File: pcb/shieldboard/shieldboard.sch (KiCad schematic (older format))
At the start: 48 parts

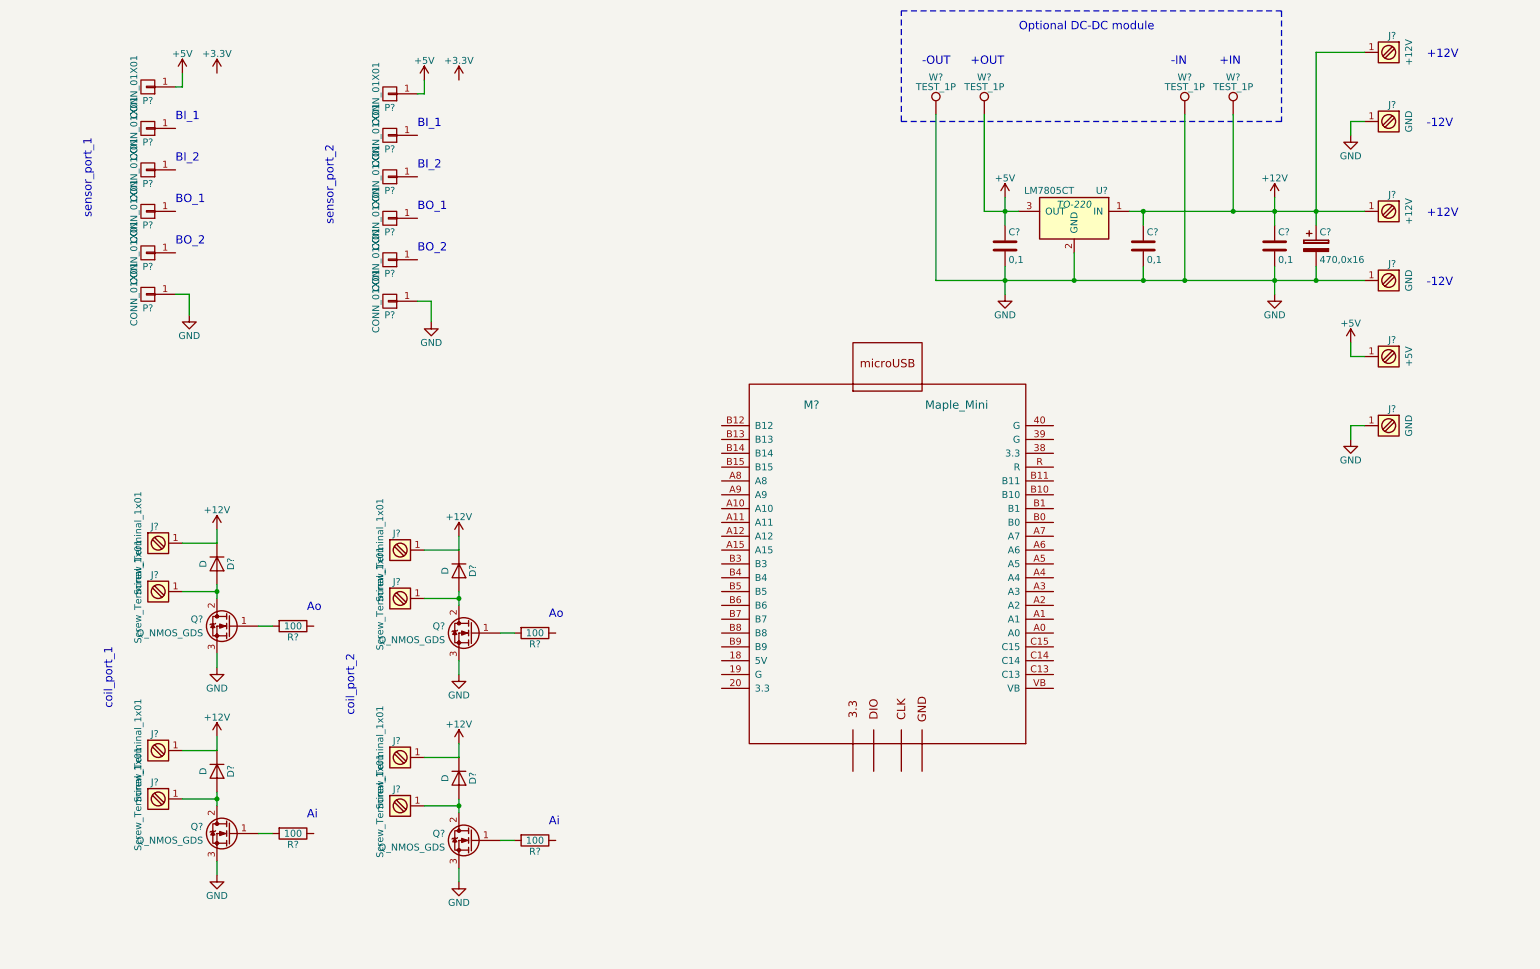
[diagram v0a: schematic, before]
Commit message: pcb: connect uC board to the shield
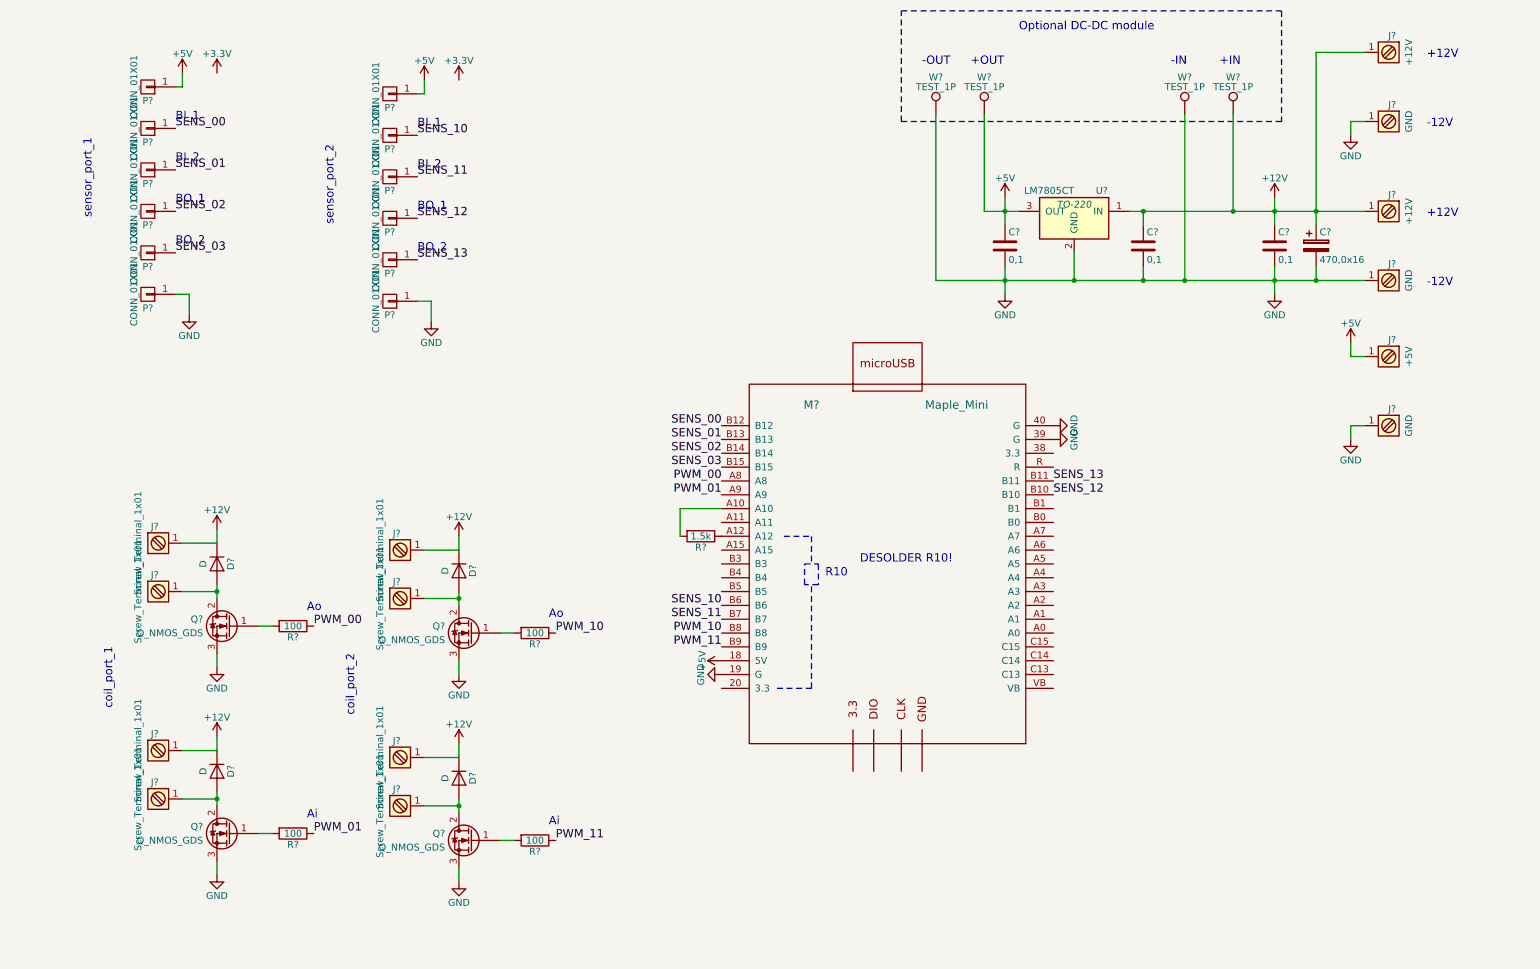
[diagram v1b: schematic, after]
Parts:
- added R?: 1.5k, symbol R
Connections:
- net +5V: now also M?.18 (5V)
- net GND: now also M?.19 (G), M?.39 (G), M?.40 (G)
- net SENS_02: now reaches P?.1 (P1)
- net SENS_02: now also M?.B14
- net SENS_01: now reaches P?.1 (P1)
- net SENS_01: now also M?.B13
- net SENS_00: now reaches P?.1 (P1)
- net SENS_00: now also M?.B12
- net SENS_03: now reaches P?.1 (P1)
- net SENS_03: now also M?.B15
- net PWM_00: now reaches R?.1
- net PWM_00: now also M?.A8
- net PWM_01: now reaches R?.1
- net PWM_01: now also M?.A9
- net at M?.A10: now also R?.2
- net at M?.A12: now also R?.1
- net SENS_12: now reaches M?.B10
- net SENS_12: now also P?.1 (P1)
- net SENS_13: now reaches M?.B11
- net SENS_13: now also P?.1 (P1)
- net SENS_10: now reaches M?.B6
- net SENS_10: now also P?.1 (P1)
- net SENS_11: now reaches M?.B7
- net SENS_11: now also P?.1 (P1)
- net PWM_10: now reaches M?.B8
- net PWM_10: now also R?.1
- net PWM_11: now reaches M?.B9
- net PWM_11: now also R?.1
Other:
- note added: "DESOLDER R10!"
- note added: "R10"
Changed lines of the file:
@@
 LIBS:memory
 LIBS:xilinx
+LIBS:special
 LIBS:microcontrollers
 LIBS:dsp
@@
 Wire Wire Line
 	10200 3350 10200 3250
+Text Label 5650 4250 2    60   ~ 0
+PWM_00
+Text Label 5650 4350 2    60   ~ 0
+PWM_01
+Text Label 5650 5350 2    60   ~ 0
+PWM_10
+Text Label 5650 5450 2    60   ~ 0
+PWM_11
+Text Label 5650 3850 2    60   ~ 0
+SENS_00
+Text Label 5650 3950 2    60   ~ 0
+SENS_01
+Text Label 5650 4050 2    60   ~ 0
+SENS_02
+Text Label 5650 4150 2    60   ~ 0
+SENS_03
+Text Label 5650 5150 2    60   ~ 0
+SENS_10
+Text Label 5650 5250 2    60   ~ 0
+SENS_11
+Text Label 8050 4350 0    60   ~ 0
+SENS_12
+Text Label 8050 4250 0    60   ~ 0
+SENS_13
+Text Label 1700 1700 0    60   ~ 0
+SENS_00
+Text Label 1700 2000 0    60   ~ 0
+SENS_01
+Text Label 1700 2300 0    60   ~ 0
+SENS_02
+Text Label 1700 2600 0    60   ~ 0
+SENS_03
+Text Label 3450 1750 0    60   ~ 0
+SENS_10
+Text Label 3450 2050 0    60   ~ 0
+SENS_11
+Text Label 3450 2350 0    60   ~ 0
+SENS_12
+Text Label 3450 2650 0    60   ~ 0
+SENS_13
+Text Label 2700 5300 0    60   ~ 0
+PWM_00
+Text Label 2700 6800 0    60   ~ 0
+PWM_01
+Text Label 4450 6850 0    60   ~ 0
+PWM_11
+Text Label 4450 5350 0    60   ~ 0
+PWM_10
+$Comp
+L GND #PWR?
+U 1 1 5B209E40
+P 8050 3850
+F 0 "#PWR?" H 8050 3600 50  0001 C CNN
+F 1 "GND" H 8050 3700 50  0000 C CNN
+F 2 "" H 8050 3850 50  0000 C CNN
+F 3 "" H 8050 3850 50  0000 C CNN
+	1    8050 3850
+	0    -1   -1   0
+$EndComp
+$Comp
+L GND #PWR?
+U 1 1 5B209EE2
+P 8050 3950
+F 0 "#PWR?" H 8050 3700 50  0001 C CNN
+F 1 "GND" H 8050 3800 50  0000 C CNN
+F 2 "" H 8050 3950 50  0000 C CNN
+F 3 "" H 8050 3950 50  0000 C CNN
+	1    8050 3950
+	0    -1   -1   0
+$EndComp
+$Comp
+L GND #PWR?
+U 1 1 5B20A0CF
+P 5650 5650
+F 0 "#PWR?" H 5650 5400 50  0001 C CNN
+F 1 "GND" H 5650 5500 50  0000 C CNN
+F 2 "" H 5650 5650 50  0000 C CNN
+F 3 "" H 5650 5650 50  0000 C CNN
+	1    5650 5650
+	0    1    1    0
+$EndComp
+$Comp
+L +5V #PWR?
+U 1 1 5B20D291
+P 5650 5550
+F 0 "#PWR?" H 5650 5400 50  0001 C CNN
+F 1 "+5V" H 5650 5690 50  0000 C CNN
+F 2 "" H 5650 5550 50  0000 C CNN
+F 3 "" H 5650 5550 50  0000 C CNN
+	1    5650 5550
+	0    -1   -1   0
+$EndComp
+$Comp
+L R R?
+U 1 1 5B20E5A1
+P 5500 4650
+F 0 "R?" V 5580 4650 50  0000 C CNN
+F 1 "1.5k" V 5500 4650 50  0000 C CNN
+F 2 "" V 5430 4650 50  0000 C CNN
+F 3 "" H 5500 4650 50  0000 C CNN
+	1    5500 4650
+	0    1    1    0
+$EndComp
+Text Notes 6650 4850 0    60   ~ 0
+DESOLDER R10!
+Wire Notes Line
+	6100 4650 6300 4650
+Wire Notes Line
+	6300 4650 6300 4850
+Wire Notes Line
+	6250 4850 6350 4850
+Wire Notes Line
+	6350 4850 6350 5000
+Wire Notes Line
+	6350 5000 6250 5000
+Wire Notes Line
+	6250 5000 6250 4850
+Wire Notes Line
+	6050 5750 6300 5750
+Wire Notes Line
+	6300 5750 6300 5000
+Text Notes 6400 4950 0    60   ~ 0
+R10
+Wire Wire Line
+	5350 4650 5350 4450
+Wire Wire Line
+	5350 4450 5650 4450
 $EndSCHEMATC

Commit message: pcb: update
Signed-off-by: Ilya Kuzmin <kuzmin.ilya@gmail.com>
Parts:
- removed C?: 470,0x16, symbol CP
- removed C? (x3): 0,1, symbol C
- removed D? (x4): D, symbol D
- removed J? (x8): Screw_Terminal_1x01, symbol Screw_Terminal_1x01
- removed J? (x3): GND, symbol Screw_Terminal_1x01
- removed J? (x2): +12V, symbol Screw_Terminal_1x01
- removed J?: +5V, symbol Screw_Terminal_1x01
- removed P? (x12): CONN_01X01, symbol CONN_01X01
- removed Q? (x4): Q_NMOS_GDS, symbol Q_NMOS_GDS
- removed R? (x4): 100, symbol R
- removed R?: 1.5k, symbol R
- removed U?: LM7805CT, TO-220, symbol LM7805CT
- removed W? (x4): TEST_1P, symbol TEST_1P
- added C1: 470,0x16, Capacitor_THT:CP_Radial_D22.0mm_P10.00mm_SnapIn, symbol Device:CP
- added C2, C3, C4: 0,1, Capacitor_SMD:C_0805_2012Metric_Pad1.29x1.40mm_HandSolder, symbol Device:C
- added C5: 10,0x16, Capacitor_THT:CP_Radial_D13.0mm_P5.00mm, symbol Device:CP
- added D1, D2, D3, D4: D, Diode_SMD:D_SMA_Handsoldering, symbol Device:D
- added J1, J2, J3, J4, J5, J6, J7: Conn_01x02, TerminalBlock:TerminalBlock_bornier-2_P5.08mm, symbol Connector_Generic:Conn_01x02
- added J10, J8: Conn_01x06, Connector_PinHeader_2.54mm:PinHeader_1x06_P2.54mm_Vertical, symbol Connector_Generic:Conn_01x06
- added J11: Conn_01x18, Connector_PinHeader_2.54mm:PinHeader_1x18_P2.54mm_Vertical, symbol Connector_Generic:Conn_01x18
- added J12: USB_B, Connector_USB:USB_B_OST_USB-B1HSxx_Horizontal, symbol Connector:USB_B
- added J13: Conn_01x01, Connector_Wire:SolderWirePad_1x01_Drill1mm, symbol Connector_Generic:Conn_01x01
- added J9: Conn_01x07, Connector_PinHeader_2.54mm:PinHeader_1x07_P2.54mm_Vertical, symbol Connector_Generic:Conn_01x07
- added M1: LM2596_DC-DC_module, ki_modules:LM2596_DC-DC_module, symbol ki_modules:LM2596_DC-DC_module
- added Q1, Q2, Q3, Q4: Q_NMOS_GDS, Package_TO_SOT_THT:TO-220-3_Vertical, symbol Device:Q_NMOS_GDS
- added R1, R2, R3, R4: 100, Resistor_SMD:R_0805_2012Metric_Pad1.29x1.40mm_HandSolder, symbol Device:R
- added R5: 1,5k, Resistor_SMD:R_0805_2012Metric_Pad1.29x1.40mm_HandSolder, symbol Device:R
- added R6, R7: 22, Resistor_SMD:R_0805_2012Metric_Pad1.15x1.40mm_HandSolder, symbol Device:R
- added U1: LM7805_TO220, Package_TO_SOT_THT:TO-220-3_Vertical, symbol Regulator_Linear:LM7805_TO220
- M2: renamed from M?; footprint (none) -> ki_modules:Maple_Mini; symbol Maple_Mini -> ki_modules:Maple_Mini
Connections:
- net labels removed: +3.3V, PWM_00, PWM_01, PWM_10, PWM_11, SENS_00, SENS_01, SENS_02, SENS_03, SENS_10, SENS_11, SENS_12, SENS_13
- wire segments 57 -> 200
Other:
- note added: "+5V"
- note added: "GND"
- note added: "PWM_00"
- note added: "PWM_01"
- note added: "PWM_10"
- note added: "PWM_11"
- note added: "SENS_00"
- note added: "SENS_01"
- note added: "SENS_02"
- note added: "SENS_03"
- note added: "SENS_10"
- note added: "SENS_11"
- note added: "SENS_12"
- note added: "SENS_13"
- note removed: "+IN"
- note removed: "+OUT"
- note removed: "-IN"
- note removed: "-OUT"
- moved on the sheet: M2
